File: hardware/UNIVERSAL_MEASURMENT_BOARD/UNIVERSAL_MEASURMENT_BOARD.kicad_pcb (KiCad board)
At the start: 6 copper layers, 75 x 95 mm, 190 parts, among them J1 2606-1110_010-000, J2 2606-1110_010-000, J3 2606-1110_010-000, J4 2606-1110_010-000, J5 Strain Relief, J6 Strain Relief, J7 FTSH-107-01-L-D-K, J8 Strain Relief, J9 Strain Relief, U1 ADS8863IDGS, U10 LT3471EDD#PBF, U11 L7812ABD2T-TR, U12 ISL21010CFH330Z-TK, U13 L78L15ACD13TR, U14 TPS54202HDDCR, U15 L79L15ACD13TR, U16 ADM3057EBRWZ, U2 STM32G484RET3, U3 PGA280AIPW, U4 CD4097BM, U5 UA78M33CDCYRG3, U6 TPS54202HDDCR, U7 UA78M33CDCYRG3, U8 L7805ABD2T-TR, U9 ISL21010CFH315Z-TK, Y1 ATX-H11-F-16.000MHz-G100-T

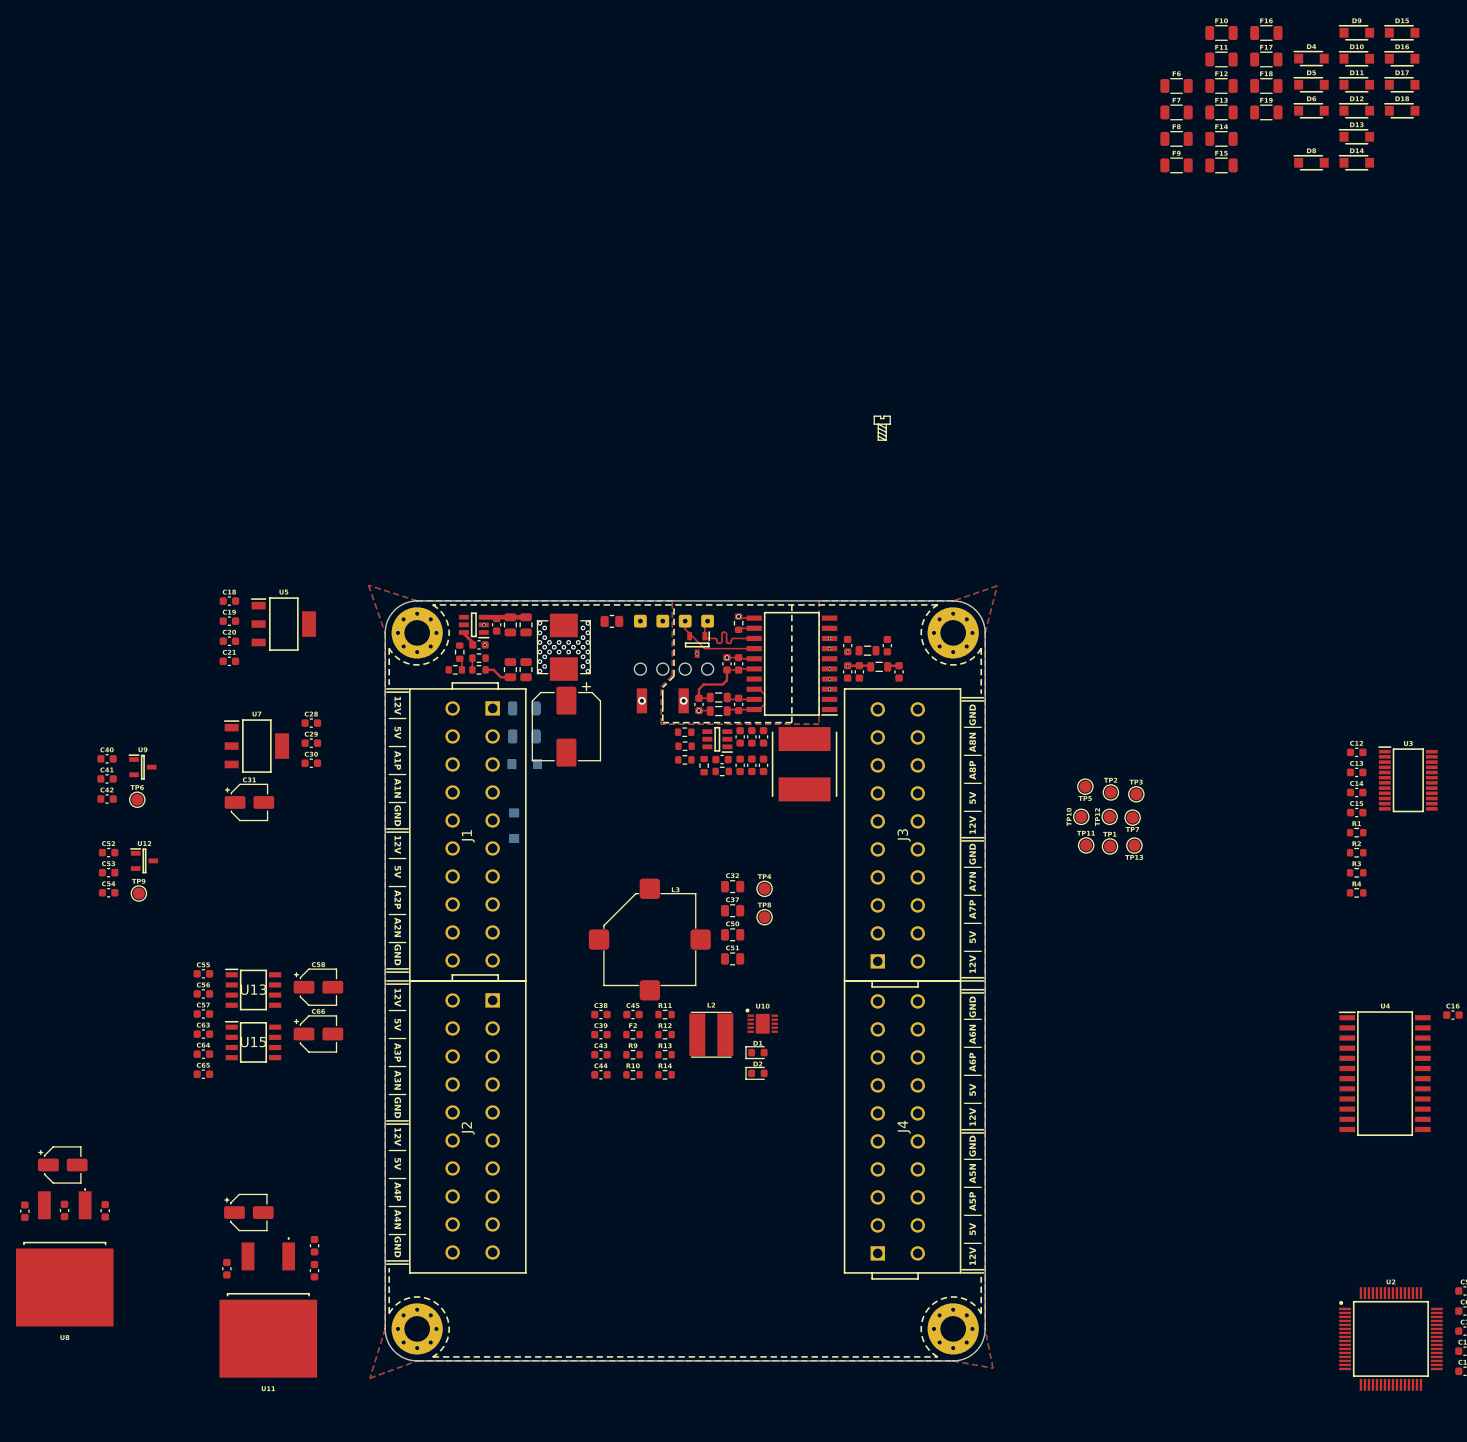
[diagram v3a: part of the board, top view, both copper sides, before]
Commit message: Update power section:
- Change input capacitor configuration to 1 per inductor in ±18V converter

- Add ±18V DC/DC, 12V LDO, and 5V LDO layouts

- Add TVS diodes and fuses to the measurement path
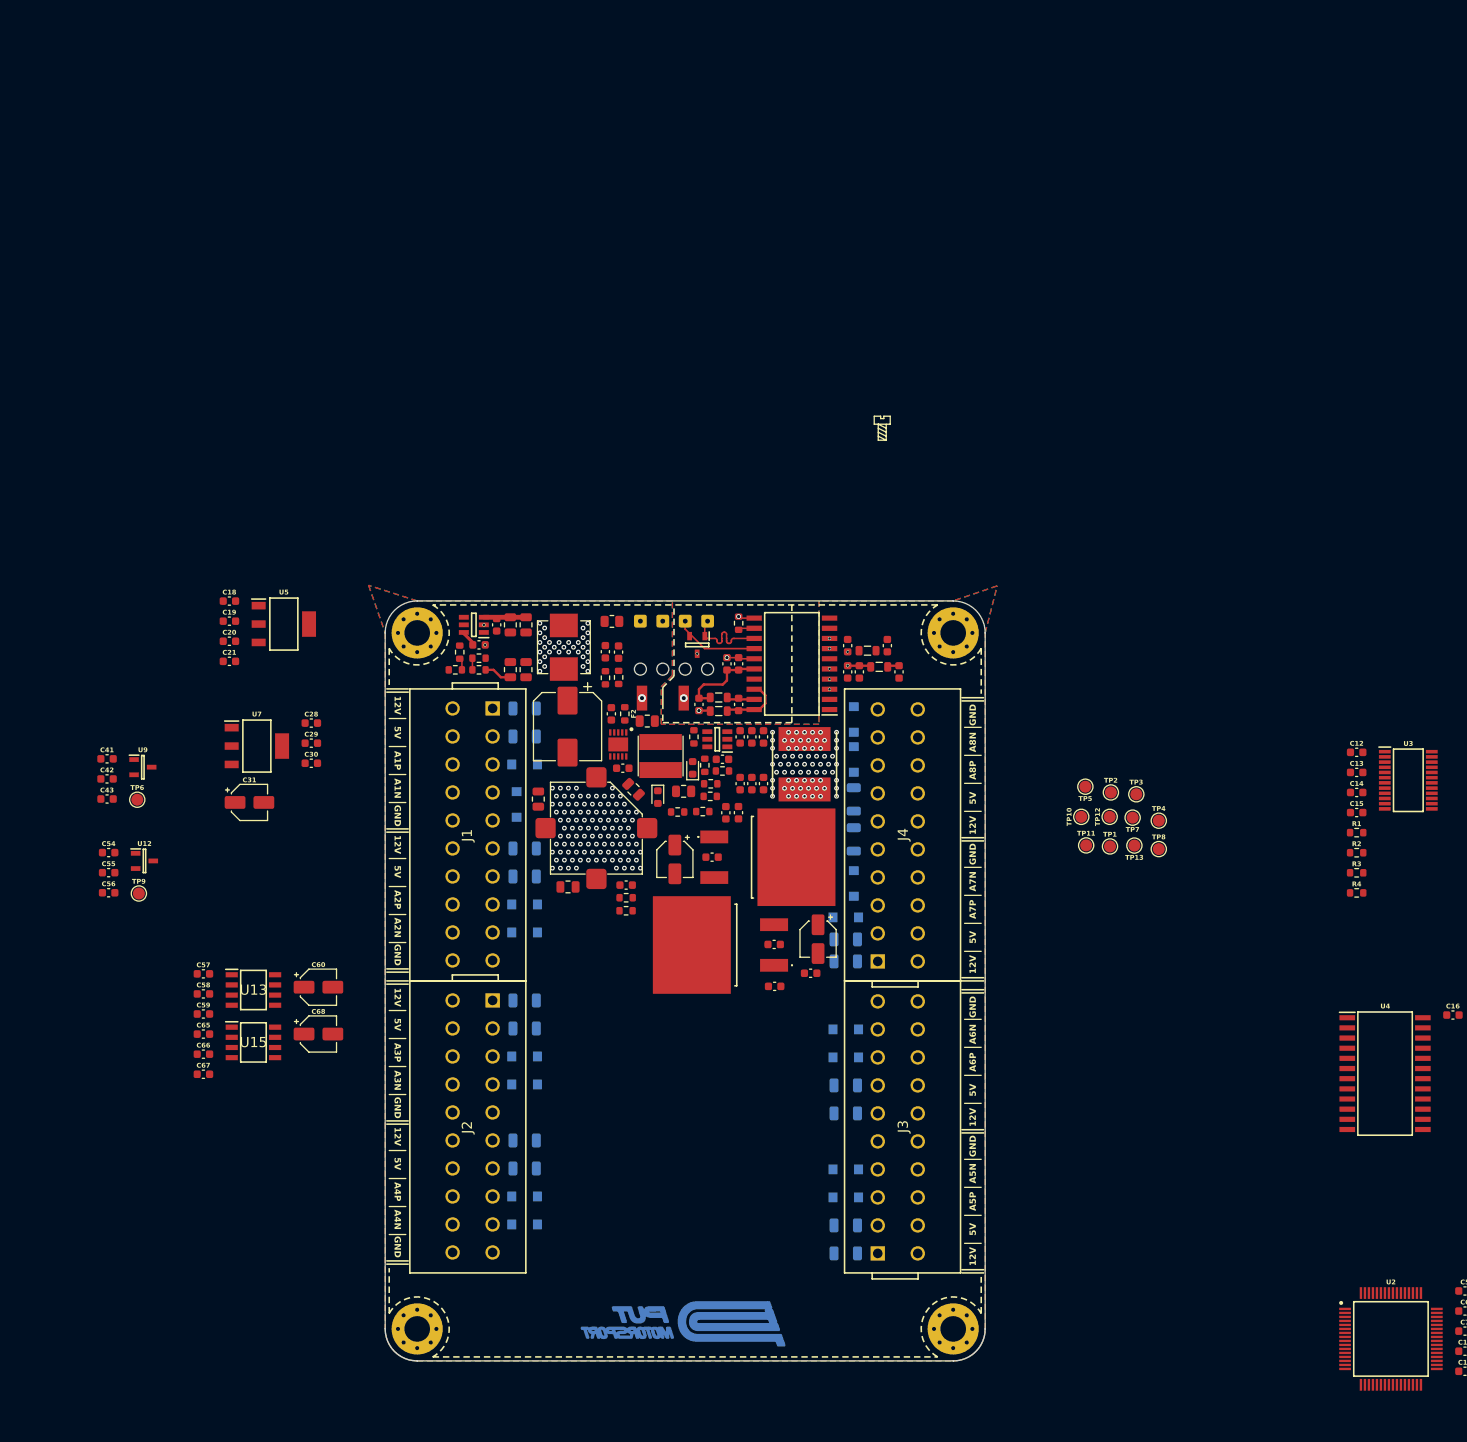
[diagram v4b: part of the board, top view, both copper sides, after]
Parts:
- removed the C37 at (80.5, 82.1)
- removed C38: 100nF, REST:C_0603_1608Metric
- removed the C43 at (64.0, 100.1)
- removed the C50 at (80.5, 85.1)
- added C33: 4.7uF, REST:C_0805_2012Metric, F.Cu at (74.3, 67.2)
- added C40: 100nF, REST:C_0603_1608Metric, F.Cu at (65.3, 57.5)
- added C46: 75pF, REST:C_0603_1608Metric, F.Cu at (67.2, 78.9)
- added C52: 10uF, REST:C_0805_2012Metric, F.Cu at (56.2, 68.2)
- added C53: 10uF, REST:C_0805_2012Metric, F.Cu at (59.9, 79.1)
- C32: value 4.7uF -> 10uF
- C45: value 75pF -> 1uF
- C51: value 10uF -> 1uF
- D10, D11, D12, D13, D14, D15, D16, D17, D18, D4, D5, D6, D8, D9, F10, F11, F12, F13, F14, F15, F16, F17, F18, F19, F6, F7, F8, F9: moved to B.Cu
- moved D16 182.4 mm to (54.5, 121.3)
- moved D12 171.0 mm to (54.5, 117.8)
- moved F17 166.8 mm to (54.5, 114.3), turned to 180 degrees
- moved D4 158.8 mm to (54.5, 100.3)
- moved D15 157.1 mm to (54.5, 84.8)
- moved F10 156.3 mm to (94.6, 121.5)
- moved D9 155.8 mm to (94.6, 114.5), turned to 180 degrees
- moved F13 155.2 mm to (54.5, 110.8), turned to 180 degrees
- moved F6 151.7 mm to (94.6, 125.0)
- moved D8 151.5 mm to (54.5, 103.8)
- moved D5 150.8 mm to (94.6, 118.0), turned to 180 degrees
- moved D11 146.0 mm to (54.5, 81.3)
- moved F16 140.4 mm to (54.5, 77.8), turned to 180 degrees
- moved D17 137.0 mm to (94.6, 97.0), turned to 180 degrees
- moved F18 135.5 mm to (94.6, 104.0)
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- renumbered C33 to C34, C34 to C35, C35 to C36, C36 to C37, C40 to C41, C41 to C42, C42 to C43, C46 to C47, C47 to C48, C48 to C49, C49 to C50, C52 to C54, C53 to C55, C54 to C56, C55 to C57, C56 to C58, C57 to C59, C58 to C60, C59 to C61, C60 to C62, C61 to C63, C62 to C64, C63 to C65, C64 to C66, C65 to C67, C66 to C68, C67 to C69, C68 to C70, C69 to C71, C70 to C72, C71 to C73, C72 to C74, C73 to C75, C74 to C76, C75 to C77, C76 to C78, C77 to C79, C78 to C80, C79 to C81
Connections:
- C32 pad 1: GND -> +14V0F
- C32 pad 2: +18V0 -> GND
- C39 pad 2: Net-(U10-FB1P) -> +14V0F
- C44 pad 2: Net-(U10-~{SHDN}/SS2) -> Net-(U10-~{SHDN}/SS1)
- C45 pad 1: -18V0 -> GND
- C45 pad 2: Net-(U10-FB2P) -> Net-(U10-~{SHDN}/SS2)
- C51 pad 1: GND -> Net-(D2-A)
- C51 pad 2: -18V0 -> Net-(U10-SW2)
- F2 pad 2: +15V0F -> +14V0F
- L2 pad 1: +15V0F -> +14V0F
- L3 pad 2: +15V0F -> +14V0F
- R11 pad 1: +15V0F -> +14V0F
- R12 pad 1: +15V0F -> +14V0F
- U10 pad 8: +15V0F -> +14V0F
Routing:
- net Net-(U14-SW): vias 0 -> 32
- net GND: vias 34 -> 147
- net +7V0: vias 0 -> 30
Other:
- board text added: "L1"
- board text added: "L6"

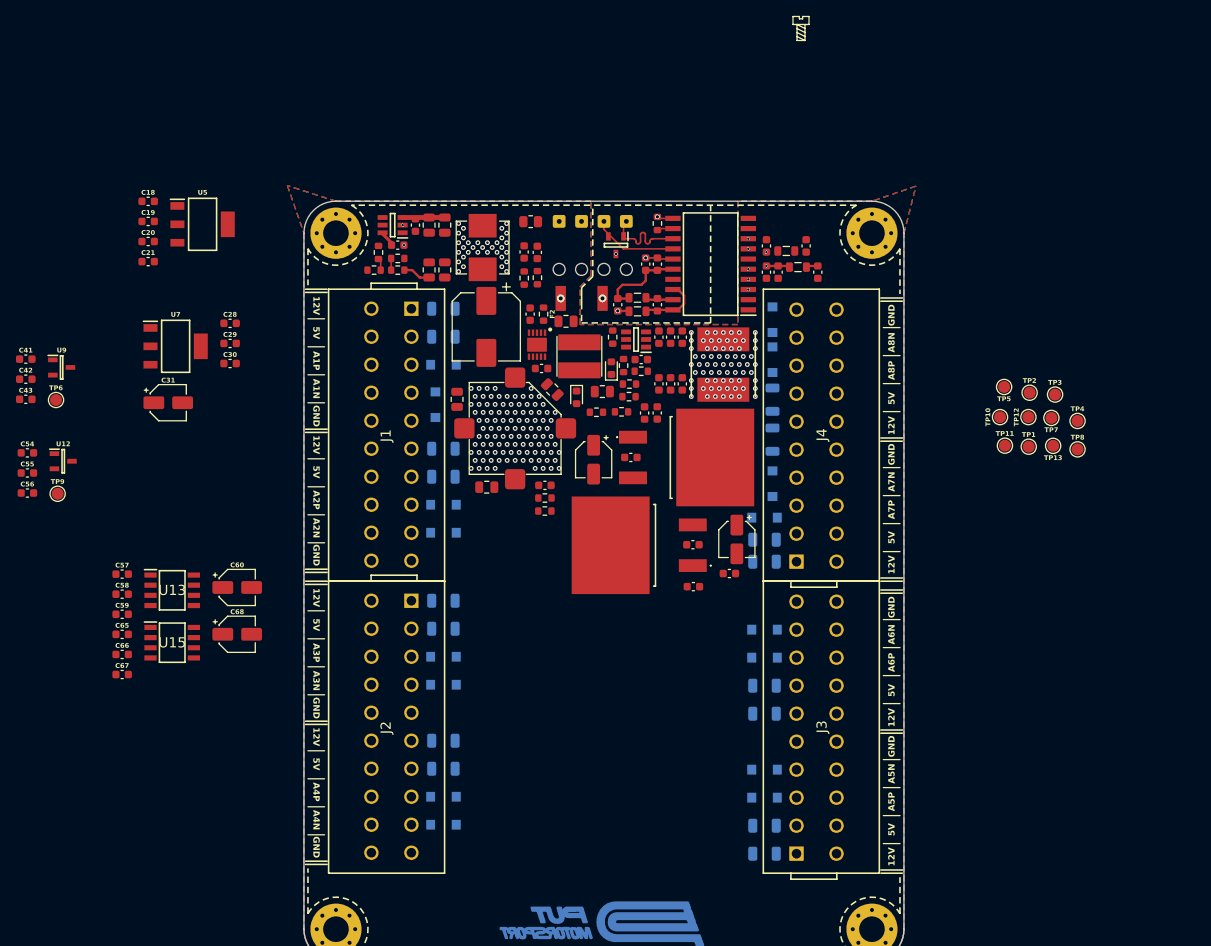
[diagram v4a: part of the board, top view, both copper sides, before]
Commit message: Finalize power section layout:
- Add dual 3.3V and ±15V LDOs

- Add 3.0V and 1.5V references

- Rework TVS and fuse placement in measurement path

- Add thermal vias to LDOs and inductors

- Improve component markings
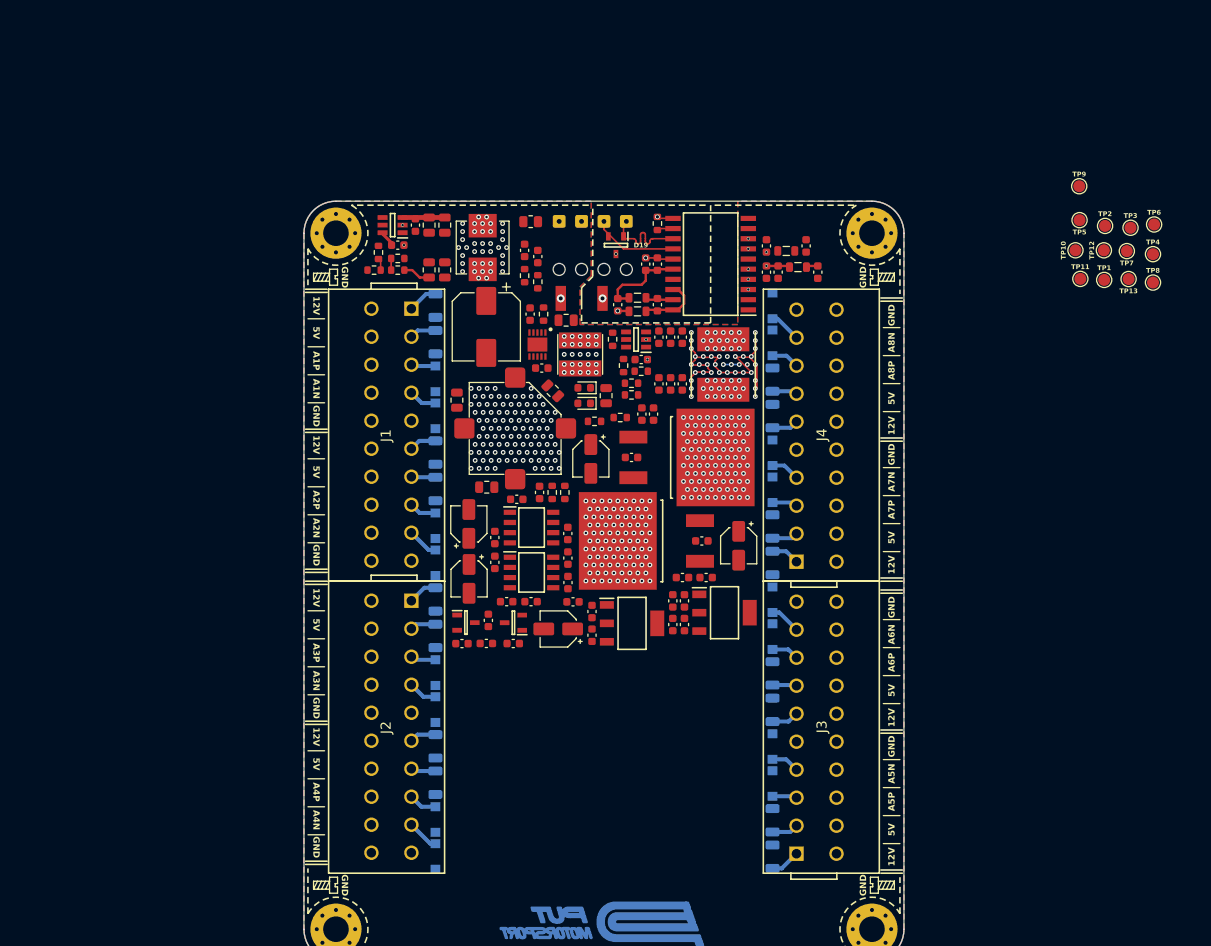
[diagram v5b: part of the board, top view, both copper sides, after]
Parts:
- removed the REF** at (99.2, 21.8)
- added REF**: Screw_Generic_2.0x3.0mm_SilkScreen, Symbol:Screw_Generic_2.0x3.0mm_SilkScreen, B.Cu at (109.3, 53.4)
- added REF**: Screw_Generic_2.0x3.0mm_SilkScreen, Symbol:Screw_Generic_2.0x3.0mm_SilkScreen, B.Cu at (39.8, 128.4)
- added REF**: Screw_Generic_2.0x3.0mm_SilkScreen, Symbol:Screw_Generic_2.0x3.0mm_SilkScreen, B.Cu at (109.3, 128.9)
- added REF**: Screw_Generic_2.0x3.0mm_SilkScreen, Symbol:Screw_Generic_2.0x3.0mm_SilkScreen, F.Cu at (109.3, 128.9)
- added REF**: Screw_Generic_2.0x3.0mm_SilkScreen, Symbol:Screw_Generic_2.0x3.0mm_SilkScreen, F.Cu at (39.8, 52.9)
- added REF**: Screw_Generic_2.0x3.0mm_SilkScreen, Symbol:Screw_Generic_2.0x3.0mm_SilkScreen, F.Cu at (109.3, 52.9)
- added REF**: Screw_Generic_2.0x3.0mm_SilkScreen, Symbol:Screw_Generic_2.0x3.0mm_SilkScreen, F.Cu at (39.8, 128.9)
- added REF**: Screw_Generic_2.0x3.0mm_SilkScreen, Symbol:Screw_Generic_2.0x3.0mm_SilkScreen, B.Cu at (39.8, 52.9)
- U11: footprint L7812ABD2T-TR:L7812ABD2TTR -> L7805ABD2T-TR:L7805ABD2TTR
- moved TP6 139.0 mm to (143.3, 46.3)
- moved TP9 133.4 mm to (134.0, 41.5)
- moved C18 83.6 mm to (84.6, 93.3), turned to -90 degrees
- moved U5 81.3 mm to (89.6, 94.8)
- moved C20 81.2 mm to (83.2, 96.3), turned to 90 degrees
- moved C21 80.9 mm to (84.6, 96.3), turned to 90 degrees
- moved C19 80.9 mm to (83.2, 93.3), turned to -90 degrees
- moved C41 70.5 mm to (63.2, 98.7), turned to 180 degrees
- moved C43 68.0 mm to (65.4, 93.5)
- moved U7 66.7 mm to (78.1, 96.2)
- moved C42 66.2 mm to (62.4, 93.5), turned to 180 degrees
- moved U9 64.9 mm to (63.2, 96.1), turned to 180 degrees
- moved C54 61.3 mm to (60.1, 95.8), turned to -90 degrees
- moved C56 60.4 mm to (59.9, 98.7)
- moved C55 58.4 mm to (56.8, 98.7), turned to 180 degrees
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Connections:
- REF** pad 1: (no net) -> GND (x4)
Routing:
- net GND: track 0.00 -> 33.5 mm, vias 147 -> 359
- net /connectors/A8N: track 0.00 -> 3.98 mm
- net /connectors/A4N: track 0.00 -> 3.98 mm
- net /connectors/A6N: track 0.00 -> 3.89 mm
- net /connectors/A2N: track 0.00 -> 3.89 mm
- net Net-(F6-Pad2): track 0.00 -> 3.76 mm
- net Net-(F4-Pad2): track 0.00 -> 3.76 mm
- net Net-(F5-Pad2): track 0.00 -> 3.67 mm
- net /connectors/A7N: track 0.00 -> 3.63 mm
- net /connectors/A3N: track 0.00 -> 3.63 mm
- net Net-(F7-Pad2): track 0.00 -> 3.54 mm
- net /connectors/A5N: track 0.00 -> 3.53 mm
- net /connectors/A1N: track 0.00 -> 3.53 mm
- net /connectors/A8P: track 0.00 -> 3.52 mm
- net /connectors/A4P: track 0.00 -> 3.52 mm
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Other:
- board text added: "C_H"
- board text added: "C_L"
- board text added: "L2"
- board text added: "U10"
- board text added: "U11"
- board text added: "VCC"
